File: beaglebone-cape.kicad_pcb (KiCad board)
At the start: 2 copper layers, 86.4 x 54.6 mm, 57 parts, among them P1 BEAGLEBONE_BLACK, Q1 2N7000, Q2 2N7000, Q3 2N7000, Q4 2N7000, U2 V7805-2000, U3 4N25, U4 4N25

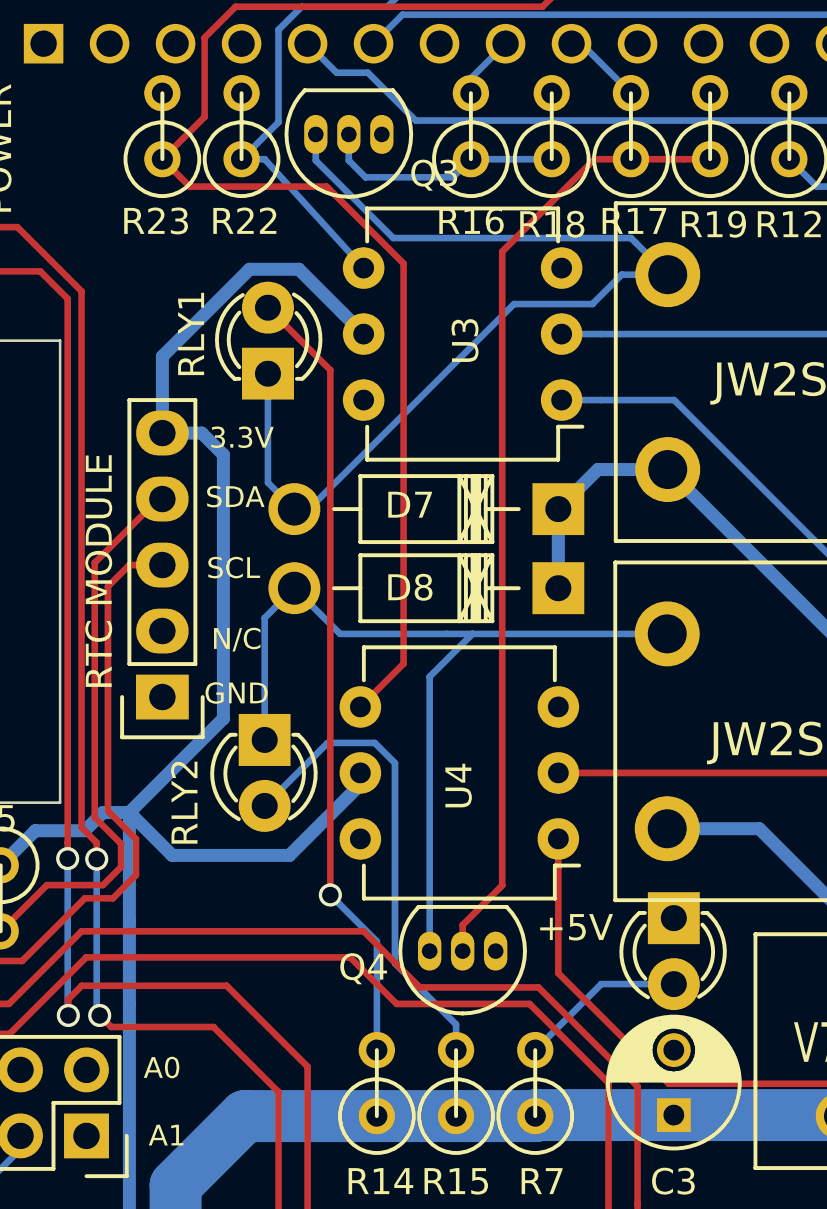
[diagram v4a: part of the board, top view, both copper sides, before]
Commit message: fixed EEPROM addressing in schmeatic, working on routing pcb now
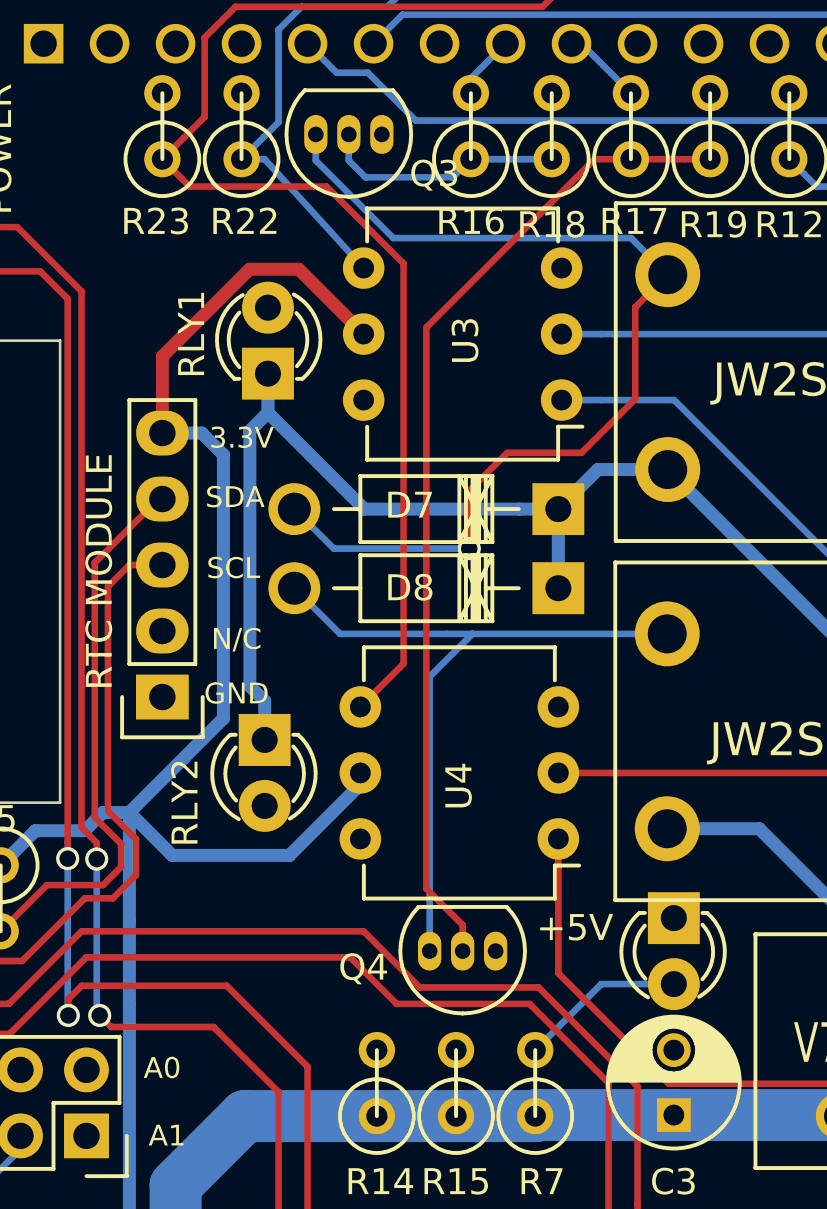
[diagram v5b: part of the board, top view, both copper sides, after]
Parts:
- RLY1, RLY2: value RELAY ON -> JW2SN-DC5V
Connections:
- RLY1 pad 1: Net-(D5-Pad1) -> +5V
- RLY1 pad 2: Net-(D5-Pad2) -> Net-(P8-Pad3)
- RLY2 pad 1: Net-(D6-Pad1) -> +5V
- RLY2 pad 2: Net-(D6-Pad2) -> Net-(P8-Pad3)
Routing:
- net Net-(D5-Pad2): track 30.3 -> 0.00 mm, vias 1 -> 0
- net +5V: track 74.4 -> 101.7 mm
- net Net-(D6-Pad2): track 18.4 -> 0.00 mm
- net Net-(D6-Pad1): track 34.3 -> 28.0 mm
- net Net-(Q4-Pad2): track 37.0 -> 38.2 mm
- net Net-(D5-Pad1): track 39.5 -> 39.1 mm, vias 0 -> 1
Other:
- net class 5V Power: trace_width 2 -> 1.5
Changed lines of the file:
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@@
   (general
     (links 128)
-    (no_connects 8)
-    (area 93.8824 84.786399 182.7236 140.1786)
+    (no_connects 2)
+    (area 94.437999 85.039999 180.898001 139.750001)
     (thickness 1.6)
     (drawings 25)
-    (tracks 365)
+    (tracks 363)
     (zones 0)
     (modules 57)
@@
   (setup
     (last_trace_width 0.254)
+    (user_trace_width 0.254)
     (user_trace_width 0.5)
     (user_trace_width 1.5)
@@
   (net_class "5V Power" ""
     (clearance 0.2286)
-    (trace_width 2)
+    (trace_width 1.5)
     (via_dia 0.889)
     (via_drill 0.635)
@@
       (effects (font (size 1 1) (thickness 0.15)))
     )
-    (fp_text value "RELAY ON" (at 1.3 -2.9 90) (layer F.Fab)
+    (fp_text value JW2SN-DC5V (at 1.3 -2.9 90) (layer F.Fab)
       (effects (font (size 1 1) (thickness 0.15)))
     )
@@
     )
     (pad 1 thru_hole rect (at 0 0 180) (size 2 2) (drill 1.00076) (layers *.Cu *.Mask F.SilkS)
-      (net 17 "Net-(D5-Pad1)"))
+      (net 10 +5V))
     (pad 2 thru_hole circle (at 2.54 0 90) (size 2 2) (drill 1.00076) (layers *.Cu *.Mask F.SilkS)
-      (net 18 "Net-(D5-Pad2)"))
+      (net 102 "Net-(P8-Pad3)"))
     (model LEDs.3dshapes/LED-3MM.wrl
       (at (xyz 0.05 0 0))
@@
       (effects (font (size 1 1) (thickness 0.15)))
     )
-    (fp_text value "RELAY ON" (at 1.3 -2.9 270) (layer F.Fab)
+    (fp_text value JW2SN-DC5V (at 1.3 -2.9 270) (layer F.Fab)
       (effects (font (size 1 1) (thickness 0.15)))
     )
@@
     )
     (pad 1 thru_hole rect (at 0 0) (size 2 2) (drill 1.00076) (layers *.Cu *.Mask F.SilkS)
-      (net 19 "Net-(D6-Pad1)"))
+      (net 10 +5V))
     (pad 2 thru_hole circle (at 2.54 0 270) (size 2 2) (drill 1.00076) (layers *.Cu *.Mask F.SilkS)
-      (net 20 "Net-(D6-Pad2)"))
+      (net 102 "Net-(P8-Pad3)"))
     (model LEDs.3dshapes/LED-3MM.wrl
       (at (xyz 0.05 0 0))
@@
   (segment (start 118.745 104.521) (end 120.261 104.521) (width 0.5) (layer B.Cu) (net 8))
   (segment (start 120.261 104.521) (end 121.0945 105.3545) (width 0.5) (layer B.Cu) (net 8))
-  (segment (start 118.745 104.521) (end 118.745 101.57067) (width 0.5) (layer B.Cu) (net 8))
-  (segment (start 118.745 101.57067) (end 122.099271 98.216399) (width 0.5) (layer B.Cu) (net 8))
-  (segment (start 122.099271 98.216399) (end 123.997399 98.216399) (width 0.5) (layer B.Cu) (net 8))
-  (segment (start 123.997399 98.216399) (end 125.692001 99.911001) (width 0.5) (layer B.Cu) (net 8))
-  (segment (start 125.692001 99.911001) (end 126.492 100.711) (width 0.5) (layer B.Cu) (net 8))
+  (segment (start 118.745 104.521) (end 118.745 101.57067) (width 0.5) (layer F.Cu) (net 8))
+  (segment (start 125.692001 99.911001) (end 126.492 100.711) (width 0.5) (layer F.Cu) (net 8))
+  (segment (start 123.997399 98.216399) (end 125.692001 99.911001) (width 0.5) (layer F.Cu) (net 8))
+  (segment (start 122.099271 98.216399) (end 123.997399 98.216399) (width 0.5) (layer F.Cu) (net 8))
+  (segment (start 118.745 101.57067) (end 122.099271 98.216399) (width 0.5) (layer F.Cu) (net 8))
   (segment (start 126.365 117.602) (end 126.365 118.0465) (width 0.5) (layer B.Cu) (net 8))
   (segment (start 126.365 118.0465) (end 123.6345 120.777) (width 0.5) (layer B.Cu) (net 8))
@@
   (segment (start 179.308601 91.278601) (end 178.079999 90.049999) (width 0.5) (layer B.Cu) (net 9))
   (segment (start 178.079999 90.049999) (end 176.93 88.9) (width 0.5) (layer B.Cu) (net 9))
+  (segment (start 122.1105 114.2605) (end 122.1105 104.4335) (width 0.5) (layer B.Cu) (net 10))
+  (segment (start 122.1105 104.4335) (end 122.809 103.735) (width 0.5) (layer B.Cu) (net 10))
+  (segment (start 122.682 116.332) (end 122.682 114.832) (width 0.5) (layer B.Cu) (net 10))
+  (segment (start 122.682 114.832) (end 122.1105 114.2605) (width 0.5) (layer B.Cu) (net 10))
+  (segment (start 122.809 102.235) (end 122.809 103.735) (width 0.5) (layer B.Cu) (net 10))
+  (segment (start 122.809 103.735) (end 126.52108 107.44708) (width 0.5) (layer B.Cu) (net 10))
+  (segment (start 126.52108 107.44708) (end 132.48551 107.44708) (width 0.5) (layer B.Cu) (net 10))
+  (segment (start 132.48551 107.44708) (end 133.985 107.44708) (width 0.5) (layer B.Cu) (net 10))
   (segment (start 133.985 110.49254) (end 133.985 107.44708) (width 0.5) (layer B.Cu) (net 10))
   (segment (start 138.195 105.925) (end 135.50708 105.925) (width 0.5) (layer B.Cu) (net 10))
@@
   (segment (start 169.1005 100.965) (end 169.1005 102.379213) (width 0.254) (layer B.Cu) (net 16))
   (segment (start 169.1005 102.379213) (end 169.1005 103.632) (width 0.254) (layer B.Cu) (net 16))
+  (segment (start 130.556 108.966) (end 125.34392 108.966) (width 0.254) (layer B.Cu) (net 17))
+  (segment (start 125.34392 108.966) (end 123.825 107.44708) (width 0.254) (layer B.Cu) (net 17))
+  (segment (start 130.556 106.7435) (end 130.556 108.966) (width 0.254) (layer F.Cu) (net 17))
+  (via (at 130.556 108.966) (size 0.889) (drill 0.635) (layers F.Cu B.Cu) (net 17))
+  (segment (start 132.0165 105.283) (end 130.556 106.7435) (width 0.254) (layer F.Cu) (net 17))
+  (segment (start 134.874 105.283) (end 132.0165 105.283) (width 0.254) (layer F.Cu) (net 17))
+  (segment (start 136.945001 103.211999) (end 134.874 105.283) (width 0.254) (layer F.Cu) (net 17))
+  (segment (start 138.195 98.425) (end 136.945001 99.674999) (width 0.254) (layer F.Cu) (net 17))
+  (segment (start 136.945001 99.674999) (end 136.945001 103.211999) (width 0.254) (layer F.Cu) (net 17))
   (segment (start 124.6505 93.0275) (end 124.6505 94.03207) (width 0.254) (layer B.Cu) (net 17))
   (segment (start 124.6505 94.03207) (end 127.633829 97.015399) (width 0.254) (layer B.Cu) (net 17))
@@
   (segment (start 136.785399 97.015399) (end 136.945001 97.175001) (width 0.254) (layer B.Cu) (net 17))
   (segment (start 136.945001 97.175001) (end 138.195 98.425) (width 0.254) (layer B.Cu) (net 17))
-  (segment (start 122.809 102.235) (end 122.809 106.43108) (width 0.254) (layer B.Cu) (net 17))
-  (segment (start 122.809 106.43108) (end 123.825 107.44708) (width 0.254) (layer B.Cu) (net 17))
-  (segment (start 136.427234 98.425) (end 138.195 98.425) (width 0.254) (layer B.Cu) (net 17))
-  (segment (start 124.38721 107.44708) (end 132.278891 99.555399) (width 0.254) (layer B.Cu) (net 17))
-  (segment (start 132.278891 99.555399) (end 135.296835 99.555399) (width 0.254) (layer B.Cu) (net 17))
-  (segment (start 135.296835 99.555399) (end 136.427234 98.425) (width 0.254) (layer B.Cu) (net 17))
-  (segment (start 125.209399 122.301) (end 125.209399 102.095399) (width 0.254) (layer F.Cu) (net 18))
-  (segment (start 127 128.27) (end 127 124.091601) (width 0.254) (layer B.Cu) (net 18))
-  (segment (start 127 124.091601) (end 125.209399 122.301) (width 0.254) (layer B.Cu) (net 18))
-  (via (at 125.209399 122.301) (size 0.889) (drill 0.635) (layers F.Cu B.Cu) (net 18))
-  (segment (start 122.809 99.695) (end 125.209399 102.095399) (width 0.254) (layer F.Cu) (net 18))
-  (segment (start 122.682 116.332) (end 122.682 111.63554) (width 0.254) (layer B.Cu) (net 19))
-  (segment (start 122.682 111.63554) (end 123.825 110.49254) (width 0.254) (layer B.Cu) (net 19))
   (segment (start 138.176 112.25) (end 130.683 112.25) (width 0.254) (layer B.Cu) (net 19))
   (segment (start 130.683 112.25) (end 129.685 112.25) (width 0.254) (layer B.Cu) (net 19))
@@
   (segment (start 129.685 112.25) (end 125.58246 112.25) (width 0.254) (layer B.Cu) (net 19))
   (segment (start 125.58246 112.25) (end 123.825 110.49254) (width 0.254) (layer B.Cu) (net 19))
-  (segment (start 130.048 128.27) (end 130.048 127.282172) (width 0.254) (layer B.Cu) (net 20))
-  (segment (start 130.048 127.282172) (end 127.698499 124.932671) (width 0.254) (layer B.Cu) (net 20))
-  (segment (start 127.698499 124.932671) (end 127.698499 117.225209) (width 0.254) (layer B.Cu) (net 20))
-  (segment (start 122.682 118.872) (end 125.107601 116.446399) (width 0.254) (layer B.Cu) (net 20))
-  (segment (start 125.107601 116.446399) (end 126.919689 116.446399) (width 0.254) (layer B.Cu) (net 20))
-  (segment (start 126.919689 116.446399) (end 127.698499 117.225209) (width 0.254) (layer B.Cu) (net 20))
   (segment (start 161.163 125.73) (end 167.5765 125.73) (width 1.5) (layer B.Cu) (net 21))
   (segment (start 167.5765 125.73) (end 169.804591 127.958091) (width 1.5) (layer B.Cu) (net 21))
@@
   (segment (start 129.921001 94.678499) (end 130.6195 93.98) (width 0.254) (layer B.Cu) (net 105))
   (segment (start 130.6195 93.98) (end 133.731 93.98) (width 0.254) (layer B.Cu) (net 105) (status 20))
-  (segment (start 131.826 97.536) (end 135.382 93.98) (width 0.254) (layer F.Cu) (net 106))
-  (segment (start 135.382 93.98) (end 136.779 93.98) (width 0.254) (layer F.Cu) (net 106))
+  (segment (start 136.779 93.98) (end 135.382 93.98) (width 0.254) (layer F.Cu) (net 106))
+  (segment (start 135.382 93.98) (end 128.905 100.457) (width 0.254) (layer F.Cu) (net 106))
+  (segment (start 128.905 100.457) (end 128.905 122.05843) (width 0.254) (layer F.Cu) (net 106))
+  (segment (start 128.905 122.05843) (end 130.302 123.45543) (width 0.254) (layer F.Cu) (net 106))
+  (segment (start 130.302 123.45543) (end 130.302 124.46) (width 0.254) (layer F.Cu) (net 106))
   (segment (start 139.827 93.98) (end 138.839172 93.98) (width 0.254) (layer F.Cu) (net 106))
   (segment (start 138.839172 93.98) (end 136.779 93.98) (width 0.254) (layer F.Cu) (net 106))
-  (segment (start 131.826 121.93143) (end 130.302 123.45543) (width 0.254) (layer F.Cu) (net 106))
-  (segment (start 131.826 97.536) (end 131.826 121.93143) (width 0.254) (layer F.Cu) (net 106))
-  (segment (start 130.302 123.45543) (end 130.302 124.46) (width 0.254) (layer F.Cu) (net 106))
   (segment (start 160.655 128.27) (end 159.667172 128.27) (width 0.254) (layer B.Cu) (net 107))
   (segment (start 159.667172 128.27) (end 158.482773 127.085601) (width 0.254) (layer B.Cu) (net 107))

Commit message: Finished pcb v1.3 and schematic v2.3
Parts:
- removed JMP: JUMPERS, Pin_Headers:Pin_Header_Straight_2x02
- removed R23: 2k, Discret:R1
- added P4: JUMPERS, Pin_Headers:Pin_Header_Straight_2x02, F.Cu at (115.8, 131.6)
- RLY1, RLY2: value JW2SN-DC5V -> RELAY ON
- moved RLY2 0.23 mm to (122.9, 116.2)
- moved RLY1 0.20 mm to (122.9, 102.0)
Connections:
- RLY1 pad 1: +5V -> Net-(D5-Pad1)
- RLY1 pad 2: Net-(P8-Pad3) -> Net-(D5-Pad2)
- RLY2 pad 1: +5V -> Net-(D6-Pad1)
- RLY2 pad 2: Net-(P8-Pad3) -> Net-(D6-Pad2)
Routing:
- net Net-(D5-Pad2): track 0.00 -> 30.8 mm, vias 0 -> 1
- net +5V: track 101.7 -> 74.4 mm
- net Net-(D6-Pad2): track 0.00 -> 18.1 mm
- net /A0: track 10.9 -> 28.6 mm
- net /A2: track 20.2 -> 11.5 mm
- net Net-(D6-Pad1): track 28.0 -> 34.1 mm
- net /A1: track 22.8 -> 26.3 mm
- net Net-(D5-Pad1): track 39.1 -> 42.4 mm
- net /LOCK_RELAYS/R2_READ: track 49.1 -> 47.5 mm
- net +3V3: track 93.8 -> 95.0 mm
